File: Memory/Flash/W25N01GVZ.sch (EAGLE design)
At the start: 1 part, among them U1 W25N01GVZEIG_TR

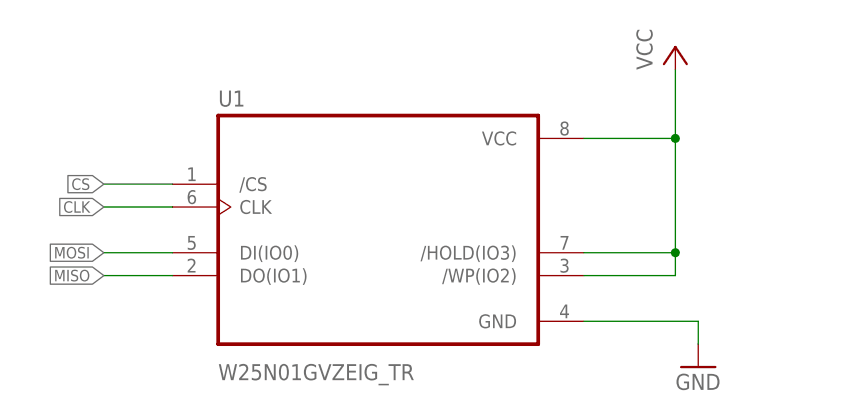
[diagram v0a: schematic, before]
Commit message: 1gb flash updated
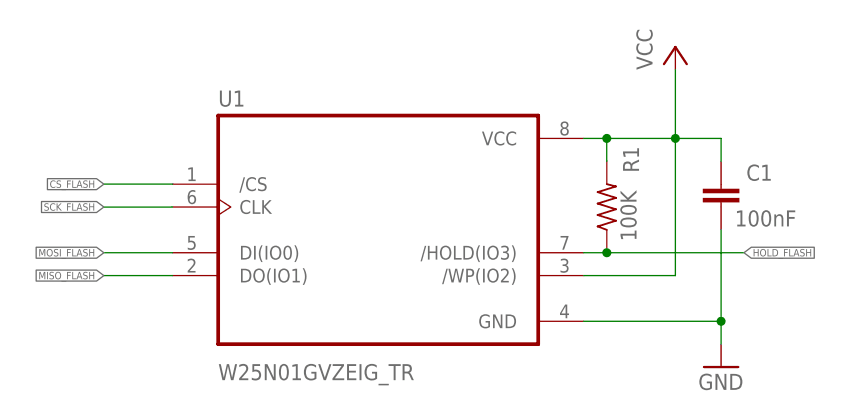
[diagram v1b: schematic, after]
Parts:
- added C1: 100nF, rcl:C-EUC0603
- added R1: 100K, rcl:R-US_R0603
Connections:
- net CLK renamed SCK_FLASH
- net CS renamed CS_FLASH
- net MISO renamed MISO_FLASH
- net MOSI renamed MOSI_FLASH
- new net HOLD_FLASH: R1.1, U1./HOLD(IO3)
- net GND: now also C1.2
- net VCC: now also C1.1, R1.2; no longer U1./HOLD(IO3)
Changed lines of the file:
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@@
 <setting verticaltext="up"/>
 </settings>
-<grid distance="0.1" unitdist="inch" unit="inch" style="lines" multiple="1" display="no" altdistance="0.01" altunitdist="inch" altunit="inch"/>
+<grid distance="0.05" unitdist="inch" unit="inch" style="lines" multiple="1" display="no" altdistance="0.01" altunitdist="inch" altunit="inch"/>
 <layers>
 <layer number="1" name="Top" color="4" fill="1" visible="no" active="no"/>
@@
 <part name="P+1" library="supply1" deviceset="VCC" device=""/>
 <part name="GND1" library="supply1" deviceset="GND" device=""/>
+<part name="C1" library="rcl" deviceset="C-EU" device="C0603" value="100nF"/>
+<part name="R1" library="rcl" deviceset="R-US_" device="R0603" value="100K"/>
 </parts>
 <sheets>
@@
 </plain>
 <instances>
-<instance part="U1" gate="G$1" x="71.12" y="63.5"/>
-<instance part="P+1" gate="VCC" x="104.14" y="83.82"/>
-<instance part="GND1" gate="1" x="106.68" y="48.26"/>
+<instance part="U1" gate="G$1" x="71.12" y="63.5" smashed="yes">
+<attribute name="NAME" x="53.34" y="77.2" size="1.778" layer="95" ratio="10" rot="SR0"/>
+<attribute name="VALUE" x="53.34" y="46.8" size="1.778" layer="96" ratio="10" rot="SR0"/>
+</instance>
+<instance part="P+1" gate="VCC" x="104.14" y="83.82" smashed="yes">
+<attribute name="VALUE" x="101.6" y="81.28" size="1.778" layer="96" rot="R90"/>
+</instance>
+<instance part="GND1" gate="1" x="109.22" y="48.26" smashed="yes">
+<attribute name="VALUE" x="106.68" y="45.72" size="1.778" layer="96"/>
+</instance>
+<instance part="C1" gate="G$1" x="109.22" y="68.58" smashed="yes">
+<attribute name="NAME" x="112.014" y="68.961" size="1.778" layer="95"/>
+<attribute name="VALUE" x="110.744" y="63.881" size="1.778" layer="96"/>
+</instance>
+<instance part="R1" gate="G$1" x="96.52" y="66.04" smashed="yes" rot="R90">
+<attribute name="NAME" x="100.1014" y="69.85" size="1.778" layer="95" rot="R90"/>
+<attribute name="VALUE" x="99.822" y="62.23" size="1.778" layer="96" rot="R90"/>
+</instance>
 </instances>
 <busses>
 </busses>
 <nets>
-<net name="CS" class="0">
+<net name="CS_FLASH" class="0">
 <segment>
 <pinref part="U1" gate="G$1" pin="/CS"/>
 <wire x1="48.26" y1="68.58" x2="40.64" y2="68.58" width="0.1524" layer="91"/>
-<label x="40.64" y="68.58" size="1.27" layer="95" rot="R180" xref="yes"/>
+<label x="40.64" y="68.58" size="0.8128" layer="95" rot="R180" xref="yes"/>
 </segment>
 </net>
-<net name="CLK" class="0">
+<net name="SCK_FLASH" class="0">
 <segment>
 <pinref part="U1" gate="G$1" pin="CLK"/>
 <wire x1="48.26" y1="66.04" x2="40.64" y2="66.04" width="0.1524" layer="91"/>
-<label x="40.64" y="66.04" size="1.27" layer="95" rot="R180" xref="yes"/>
+<label x="40.64" y="66.04" size="0.8128" layer="95" rot="R180" xref="yes"/>
 </segment>
 </net>
-<net name="MOSI" class="0">
+<net name="MOSI_FLASH" class="0">
 <segment>
 <pinref part="U1" gate="G$1" pin="DI(IO0)"/>
 <wire x1="48.26" y1="60.96" x2="40.64" y2="60.96" width="0.1524" layer="91"/>
-<label x="40.64" y="60.96" size="1.27" layer="95" rot="R180" xref="yes"/>
+<label x="40.64" y="60.96" size="0.8128" layer="95" rot="R180" xref="yes"/>
 </segment>
 </net>
-<net name="MISO" class="0">
+<net name="MISO_FLASH" class="0">
 <segment>
 <pinref part="U1" gate="G$1" pin="DO(IO1)"/>
 <wire x1="48.26" y1="58.42" x2="40.64" y2="58.42" width="0.1524" layer="91"/>
-<label x="40.64" y="58.42" size="1.27" layer="95" rot="R180" xref="yes"/>
+<label x="40.64" y="58.42" size="0.8128" layer="95" rot="R180" xref="yes"/>
 </segment>
 </net>
@@
 <segment>
 <pinref part="GND1" gate="1" pin="GND"/>
-<wire x1="106.68" y1="50.8" x2="106.68" y2="53.34" width="0.1524" layer="91"/>
+<wire x1="109.22" y1="50.8" x2="109.22" y2="53.34" width="0.1524" layer="91"/>
 <pinref part="U1" gate="G$1" pin="GND"/>
-<wire x1="93.98" y1="53.34" x2="106.68" y2="53.34" width="0.1524" layer="91"/>
+<wire x1="93.98" y1="53.34" x2="109.22" y2="53.34" width="0.1524" layer="91"/>
+<pinref part="C1" gate="G$1" pin="2"/>
+<wire x1="109.22" y1="63.5" x2="109.22" y2="53.34" width="0.1524" layer="91"/>
+<junction x="109.22" y="53.34"/>
 </segment>
 </net>
@@
 <wire x1="93.98" y1="58.42" x2="104.14" y2="58.42" width="0.1524" layer="91"/>
 <pinref part="P+1" gate="VCC" pin="VCC"/>
-<wire x1="104.14" y1="58.42" x2="104.14" y2="60.96" width="0.1524" layer="91"/>
 <pinref part="U1" gate="G$1" pin="VCC"/>
-<wire x1="104.14" y1="60.96" x2="104.14" y2="73.66" width="0.1524" layer="91"/>
+<wire x1="104.14" y1="58.42" x2="104.14" y2="73.66" width="0.1524" layer="91"/>
 <wire x1="104.14" y1="73.66" x2="104.14" y2="81.28" width="0.1524" layer="91"/>
-<wire x1="93.98" y1="73.66" x2="104.14" y2="73.66" width="0.1524" layer="91"/>
+<wire x1="93.98" y1="73.66" x2="96.52" y2="73.66" width="0.1524" layer="91"/>
 <junction x="104.14" y="73.66"/>
-<pinref part="U1" gate="G$1" pin="/HOLD(IO3)"/>
-<wire x1="93.98" y1="60.96" x2="104.14" y2="60.96" width="0.1524" layer="91"/>
-<junction x="104.14" y="60.96"/>
+<pinref part="C1" gate="G$1" pin="1"/>
+<wire x1="96.52" y1="73.66" x2="104.14" y2="73.66" width="0.1524" layer="91"/>
+<wire x1="104.14" y1="73.66" x2="109.22" y2="73.66" width="0.1524" layer="91"/>
+<wire x1="109.22" y1="73.66" x2="109.22" y2="71.12" width="0.1524" layer="91"/>
+<pinref part="R1" gate="G$1" pin="2"/>
+<wire x1="96.52" y1="71.12" x2="96.52" y2="73.66" width="0.1524" layer="91"/>
+<junction x="96.52" y="73.66"/>
 </segment>
 </net>
+<net name="HOLD_FLASH" class="0">
+<segment>
+<pinref part="U1" gate="G$1" pin="/HOLD(IO3)"/>
+<pinref part="R1" gate="G$1" pin="1"/>
+<wire x1="93.98" y1="60.96" x2="96.52" y2="60.96" width="0.1524" layer="91"/>
+<wire x1="96.52" y1="60.96" x2="111.76" y2="60.96" width="0.1524" layer="91"/>
+<junction x="96.52" y="60.96"/>
+<label x="111.76" y="60.96" size="0.8128" layer="95" xref="yes"/>
+</segment>
+</net>
